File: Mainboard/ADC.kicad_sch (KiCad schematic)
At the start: 19 parts, among them U10 TL072, U11 ADG419BR, U12 ADG419BR, U8 LTC2326CMS-16-PBF, U9 LT1469CS8-TRPBF

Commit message: Mainboard grind
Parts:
- added JP30, JP31, JP32, JP33: Jumper, Jumper:SolderJumper-2_P1.3mm_Open_TrianglePad1.0x1.5mm, symbol Mainboard-rescue:Jumper-Device
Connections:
- net AIN+: now also JP32.1
- net AIN-: now also JP33.1
- net GND: now also JP32.2, JP33.2
- net T_Amp+: now also JP30.1
- net T_Amp-: now also JP31.1
- net at R59.1, U11.1: now also JP30.2
- net at R62.1, U12.1: now also JP31.2
- net CNV renamed CNV_ADC
- net ~CS_ADC renamed CS_ADC

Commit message: working mainboard push!
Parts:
- C29, C30, C31, C32: footprint (none) -> Capacitor_SMD:C_0805_2012Metric; Mouser Part Number (none) -> 80-C0805C332KCR
- C33: footprint (none) -> Capacitor_SMD:C_0805_2012Metric; Mouser Part Number (none) -> 80-C0805C476M9P7800
- C34, C36: footprint (none) -> Capacitor_SMD:C_0805_2012Metric; Mouser Part Number (none) -> 80-C0805S104K1RACAUT
- C35: footprint (none) -> Capacitor_THT:CP_Radial_D5.0mm_P2.00mm; Mouser Part Number (none) -> 710-860020472003
- R59, R61, R62, R63: footprint (none) -> Resistor_SMD:R_0805_2012Metric; Mouser Part Number (none) -> 667-ERA-6AEB471V
- R60: footprint (none) -> Resistor_SMD:R_0805_2012Metric; Mouser Part Number (none) -> 708-RNCA0805BTE100R
- R64: footprint (none) -> Resistor_SMD:R_0805_2012Metric; Mouser Part Number (none) -> 755-ESR10EZPD1002
- U10: footprint (none) -> Package_SO:SOIC-8-1EP_3.9x4.9mm_P1.27mm_EP2.29x3mm_ThermalVias; Mouser Part Number (none) -> 511-TL072BIDT
- U11, U12: Mouser Part Number (none) -> 584-ADG419BRZ-R
- U8: Mouser Part Number (none) -> 584-LTC2326CMS-16PBF
- U9: Mouser Part Number (none) -> 584-LT1469CS8#TRPBF
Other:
- note added: "Buffer (for readout)"
- note added: "If soldered Lock-In Amps, but don't want functionality"
- note added: "Install one of these Jumpers (JP30/31) OR Lock-In Amps (U11/U12)"
- moved on the sheet: C29, C30, C31, C32, C33, C34, C35, C36, JP30, JP31, JP32, JP33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

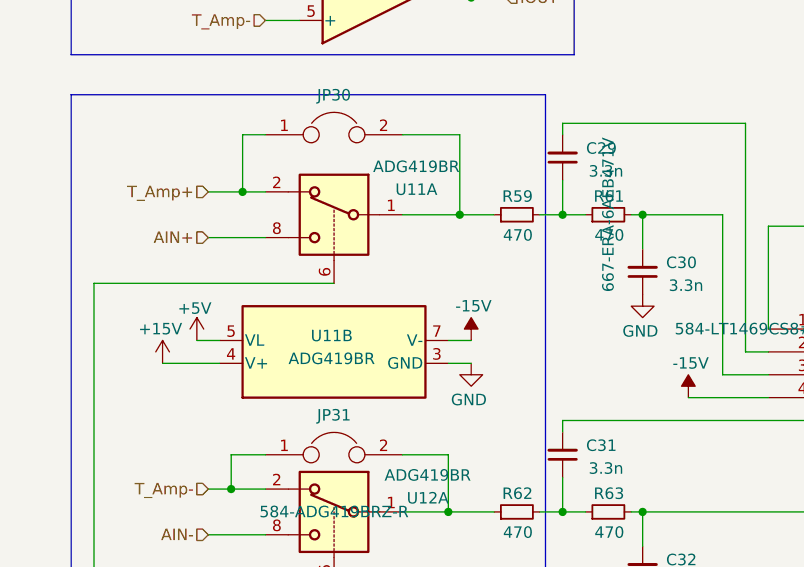
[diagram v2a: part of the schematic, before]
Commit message: mainboard working commits!
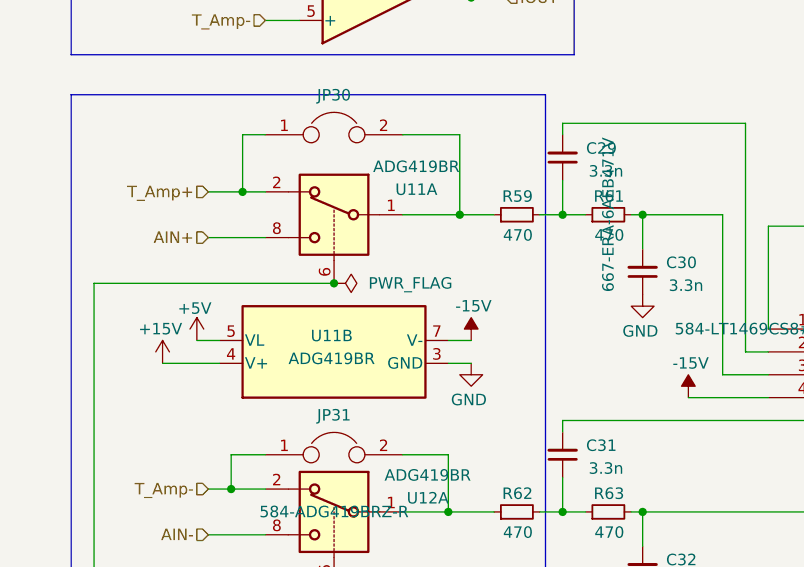
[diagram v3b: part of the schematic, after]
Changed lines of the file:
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@@
 	)
 	(junction
+		(at 68.58 107.95)
+		(diameter 0)
+		(color 0 0 0 0)
+	)
+	(junction
 		(at 58.42 97.79)
 		(diameter 0)
@@
 					(unit 1)
 				)
+			)
+		)
+	)
+	(symbol
+		(lib_id "power:PWR_FLAG")
+		(at 68.58 107.95 270)
+		(unit 1)
+		(exclude_from_sim no)
+		(in_bom yes)
+		(on_board yes)
+		(dnp no)
+		(fields_autoplaced yes)
+		(property "Reference" "#FLG06"
+			(at 70.485 107.95 0)
+			(effects
+				(font
+					(size 1.27 1.27)
+				)
+				(hide yes)
+			)
+		)
+		(property "Value" "PWR_FLAG"
+			(at 72.39 107.9499 90)
+			(effects
+				(font
+					(size 1.27 1.27)
+				)
+				(justify left)
+			)
+		)
+		(property "Footprint" ""
+			(at 68.58 107.95 0)
+			(effects
+				(font
+					(size 1.27 1.27)
+				)
+				(hide yes)
+			)
+		)
+		(property "Datasheet" "~"
+			(at 68.58 107.95 0)
+			(effects
+				(font
+					(size 1.27 1.27)
+				)
+				(hide yes)
+			)
+		)
+		(property "Description" "Special symbol for telling ERC where power comes from"
+			(at 68.58 107.95 0)
+			(effects
+				(font
+					(size 1.27 1.27)
+				)
+				(hide yes)
+			)
+		)
+		(pin "1"
+		)
+		(instances
+			(project "Mainboard"
+				(path "/6062de0a-19b5-4384-b464-187ca20917ea/ea3d873f-ee3e-4e9e-9cbb-6c2bbebc39b0"
+					(reference "#FLG06")
+					(unit 1)
+				)

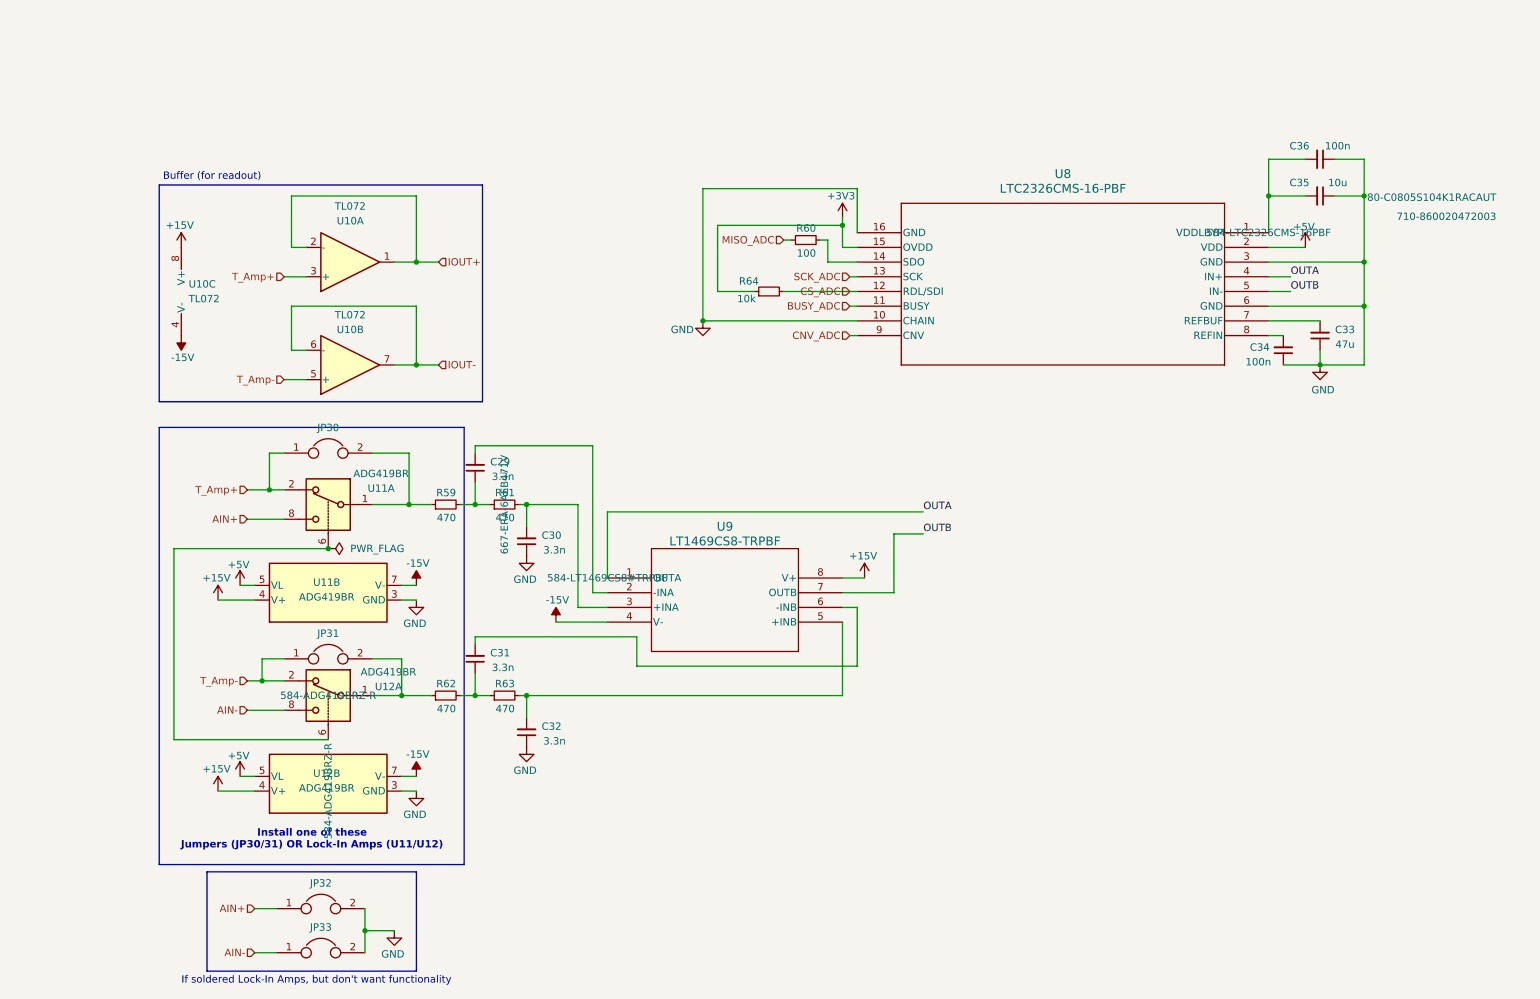
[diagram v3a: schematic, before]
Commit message: updates to DAC + ADC Libraries
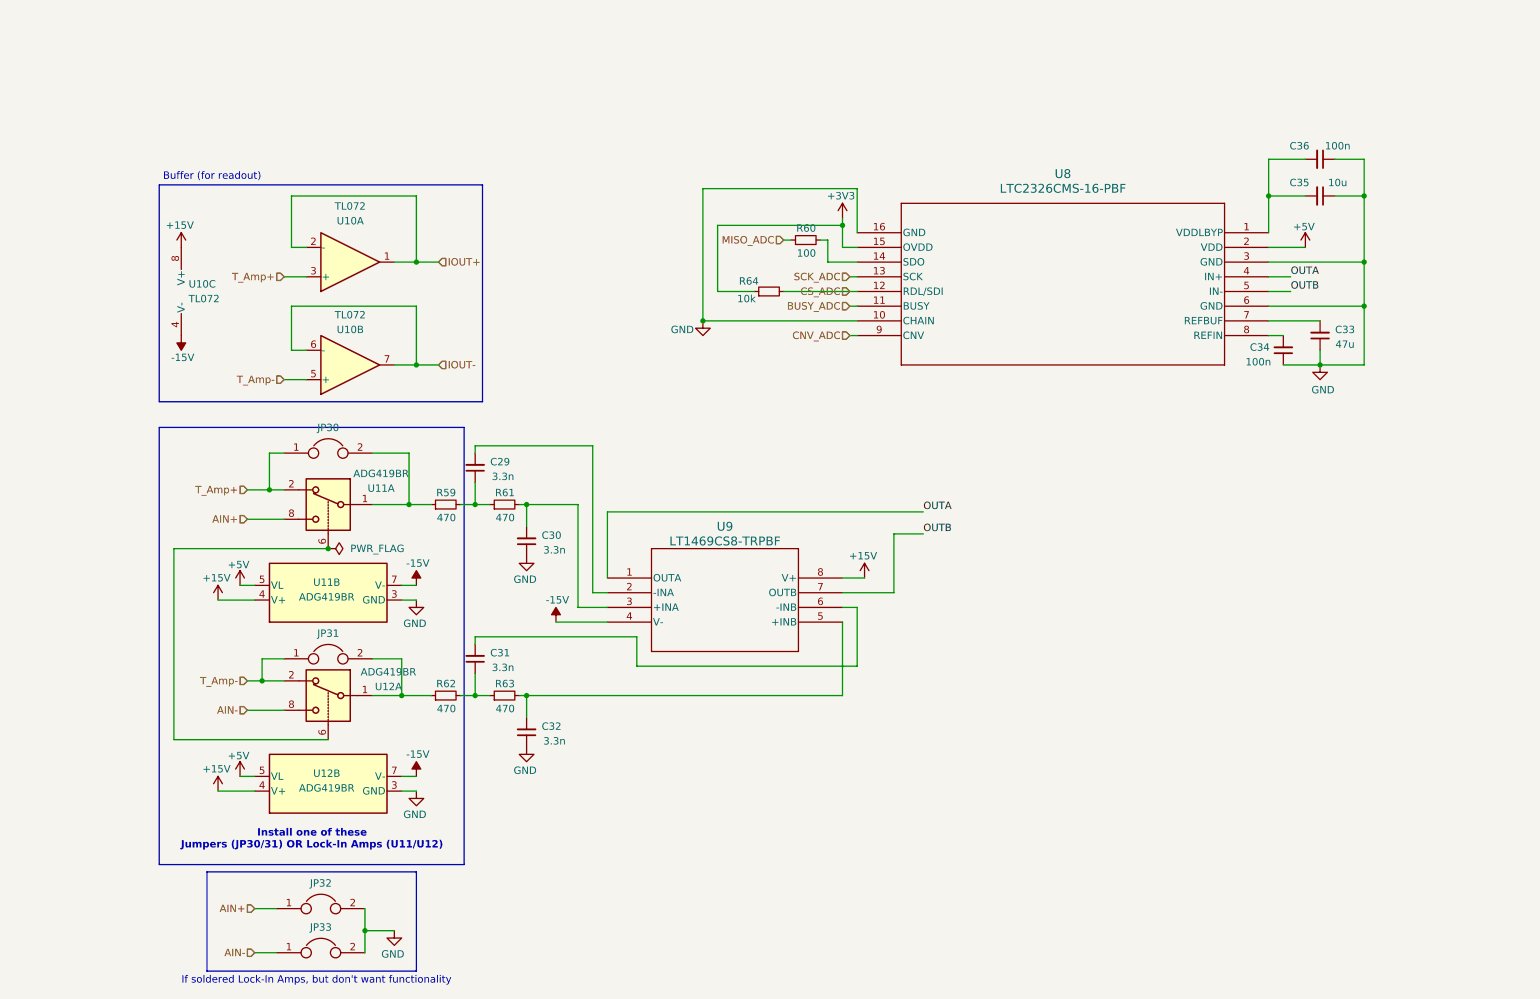
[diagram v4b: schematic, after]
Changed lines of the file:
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@@
 					(size 1.27 1.27)
 				)
+				(hide yes)
 			)
 		)
@@
 		)
 		(property "Mouser Part Number" "710-860020472003 "
-			(at 261.874 50.546 90)
-			(effects
-				(font
-					(size 1.27 1.27)
-				)
+			(at 263.652 54.864 90)
+			(effects
+				(font
+					(size 1.27 1.27)
+				)
+				(hide yes)
 			)
 		)
@@
 					(size 1.27 1.27)
 				)
+				(hide yes)
 			)
 		)
@@
 					(size 1.27 1.27)
 				)
+				(hide yes)
 			)
 		)
@@
 					(size 1.27 1.27)
 				)
+				(hide yes)
 			)
 		)
@@
 					(size 1.27 1.27)
 				)
+				(hide yes)
 			)
 		)
@@
 					(size 1.27 1.27)
 				)
-			)
-		)
+				(hide yes)
+			)
+		)
